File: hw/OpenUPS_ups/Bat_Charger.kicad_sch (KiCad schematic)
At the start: 23 parts, among them Q501 Q_PMOS_GDS, U501 MCP1415, U502 INA181A3, U503 MCP6001R, U504 MCP6001R

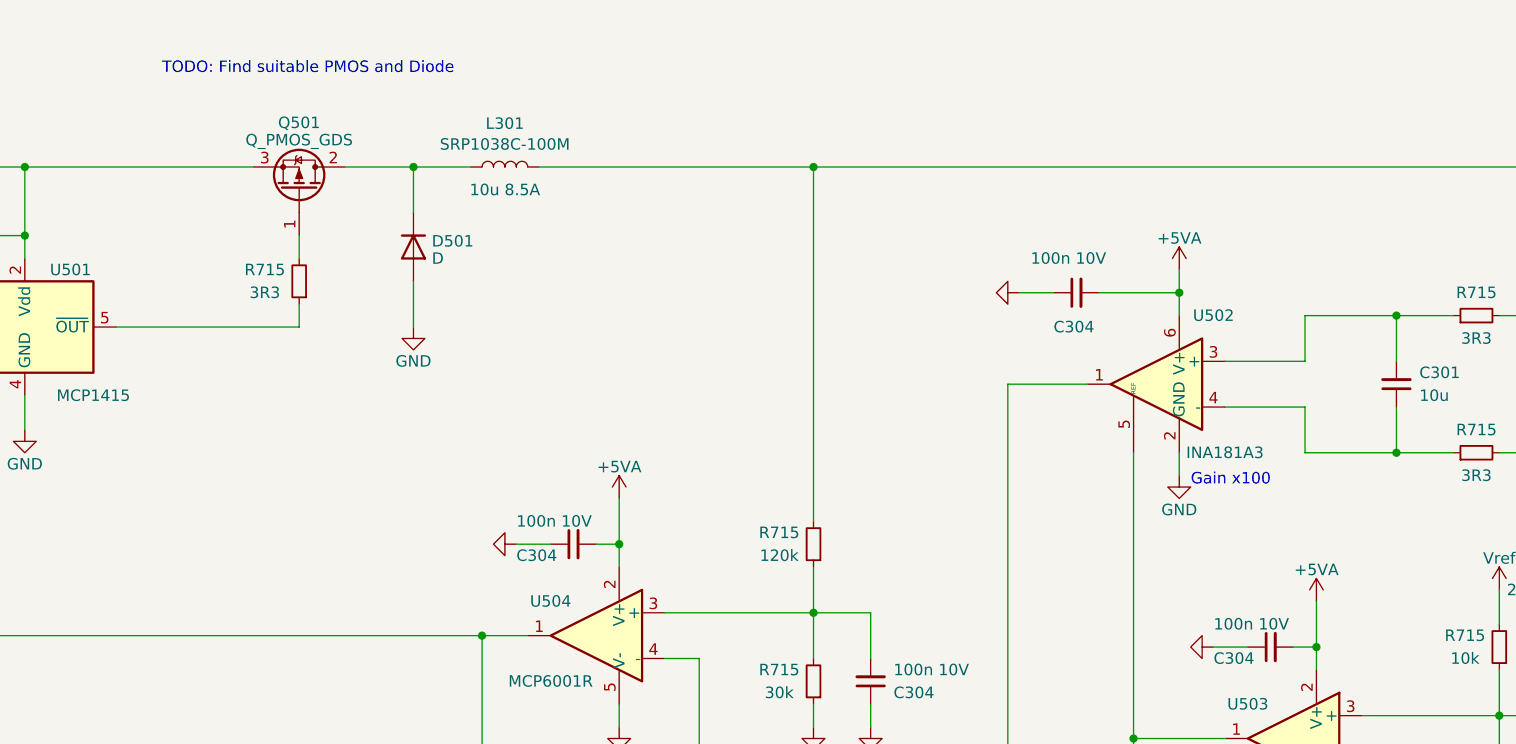
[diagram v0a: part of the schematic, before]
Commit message: Secondary blocks design
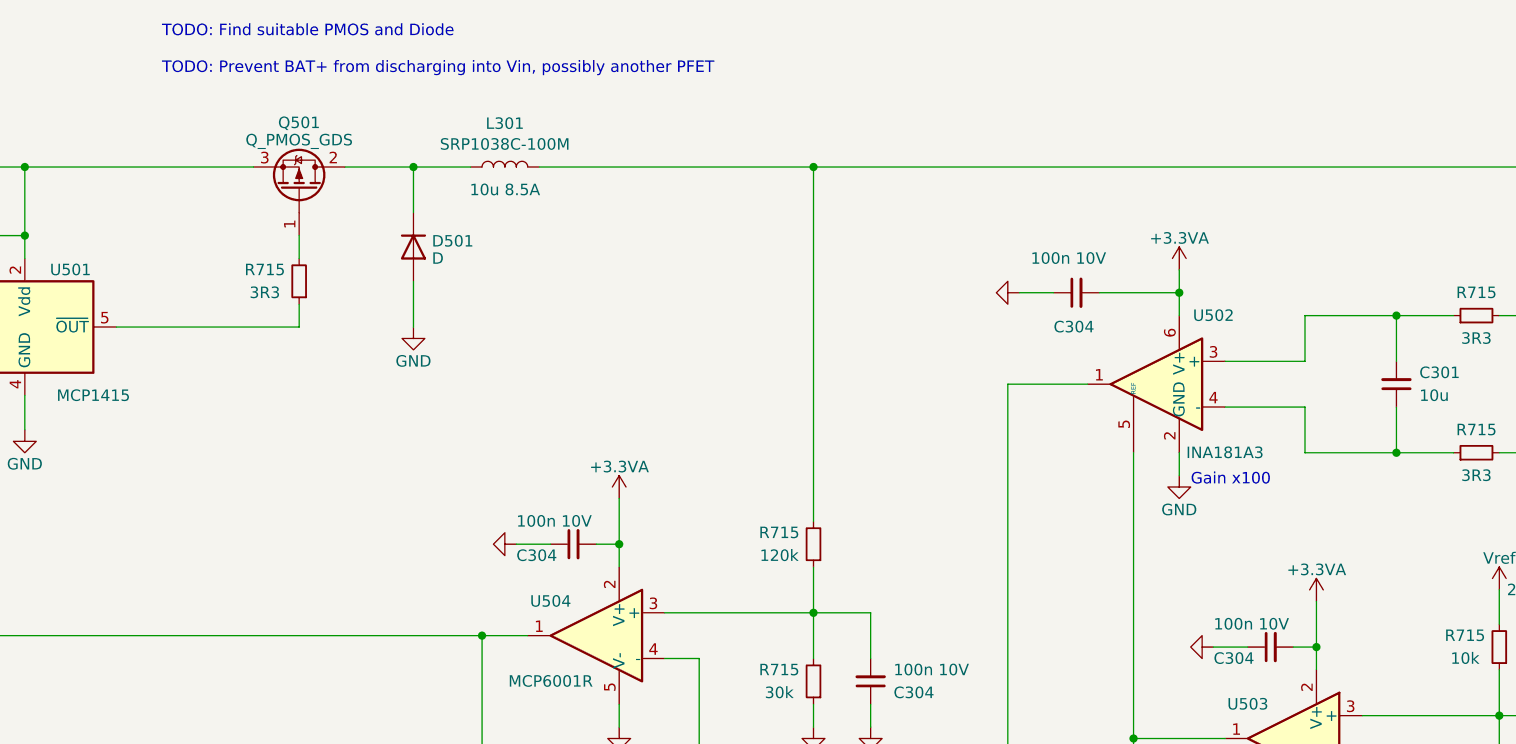
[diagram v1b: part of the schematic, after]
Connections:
- net +5VA renamed +3.3VA
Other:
- note added: "TODO: Find suitable PMOS and Diode TODO: Prevent BAT+ from discharging into Vin, possibly another PFET"
- note removed: "TODO: Find suitable PMOS and Diode"
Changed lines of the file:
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@@
     (effects (font (size 1.27 1.27)) (justify left bottom))
   )
-  (text "TODO: Find suitable PMOS and Diode" (at 95.25 62.23 0)
+  (text "TODO: Find suitable PMOS and Diode\n\nTODO: Prevent BAT+ from discharging into Vin, possibly another PFET"
+    (at 95.25 62.23 0)
     (effects (font (size 1.27 1.27)) (justify left bottom))
   )
@@
     )
   )
+  (symbol (lib_id "power:+3.3VA") (at 146.05 109.22 0) (unit 1)
+    (in_bom yes) (on_board yes) (dnp no) (fields_autoplaced)
+    (property "Reference" "#PWR0102" (at 146.05 113.03 0)
+      (effects (font (size 1.27 1.27)) hide)
+    )
+    (property "Value" "+3.3VA" (at 146.05 105.7181 0)
+      (effects (font (size 1.27 1.27)))
+    )
+    (property "Footprint" "" (at 146.05 109.22 0)
+      (effects (font (size 1.27 1.27)) hide)
+    )
+    (property "Datasheet" "" (at 146.05 109.22 0)
+      (effects (font (size 1.27 1.27)) hide)
+    )
+    (pin "1")
+    (instances
+      (project "OpenUPS_ups"
+        (path "/f77faec3-eac4-47f3-a2de-ec4a039f4502"
+          (reference "#PWR0102") (unit 1)
+        )
+        (path "/f77faec3-eac4-47f3-a2de-ec4a039f4502/0bd99307-a15c-41e8-997b-077d576f806c"
+          (reference "#PWR0431") (unit 1)
+        )
+      )
+    )
+  )
   (symbol (lib_id "power:GND") (at 190.5 86.36 270) (unit 1)
     (in_bom yes) (on_board yes) (dnp no)
@@
         (path "/f77faec3-eac4-47f3-a2de-ec4a039f4502/0bd99307-a15c-41e8-997b-077d576f806c"
           (reference "U504") (unit 1)
+        )
+      )
+    )
+  )
+  (symbol (lib_id "power:+3.3VA") (at 223.52 120.65 0) (unit 1)
+    (in_bom yes) (on_board yes) (dnp no) (fields_autoplaced)
+    (property "Reference" "#PWR0102" (at 223.52 124.46 0)
+      (effects (font (size 1.27 1.27)) hide)
+    )
+    (property "Value" "+3.3VA" (at 223.52 117.1481 0)
+      (effects (font (size 1.27 1.27)))
+    )
+    (property "Footprint" "" (at 223.52 120.65 0)
+      (effects (font (size 1.27 1.27)) hide)
+    )
+    (property "Datasheet" "" (at 223.52 120.65 0)
+      (effects (font (size 1.27 1.27)) hide)
+    )
+    (pin "1")
+    (instances
+      (project "OpenUPS_ups"
+        (path "/f77faec3-eac4-47f3-a2de-ec4a039f4502"
+          (reference "#PWR0102") (unit 1)
+        )
+        (path "/f77faec3-eac4-47f3-a2de-ec4a039f4502/0bd99307-a15c-41e8-997b-077d576f806c"
+          (reference "#PWR0433") (unit 1)
         )
       )
@@
     )
   )
+  (symbol (lib_id "power:+3.3VA") (at 208.28 83.82 0) (unit 1)
+    (in_bom yes) (on_board yes) (dnp no) (fields_autoplaced)
+    (property "Reference" "#PWR0102" (at 208.28 87.63 0)
+      (effects (font (size 1.27 1.27)) hide)
+    )
+    (property "Value" "+3.3VA" (at 208.28 80.3181 0)
+      (effects (font (size 1.27 1.27)))
+    )
+    (property "Footprint" "" (at 208.28 83.82 0)
+      (effects (font (size 1.27 1.27)) hide)
+    )
+    (property "Datasheet" "" (at 208.28 83.82 0)
+      (effects (font (size 1.27 1.27)) hide)
+    )
+    (pin "1")
+    (instances
+      (project "OpenUPS_ups"
+        (path "/f77faec3-eac4-47f3-a2de-ec4a039f4502"
+          (reference "#PWR0102") (unit 1)
+        )
+        (path "/f77faec3-eac4-47f3-a2de-ec4a039f4502/0bd99307-a15c-41e8-997b-077d576f806c"
+          (reference "#PWR0432") (unit 1)
+        )
+      )
+    )
+  )
   (symbol (lib_id "power:GND") (at 212.09 125.73 270) (unit 1)
     (in_bom yes) (on_board yes) (dnp no)
@@
         (path "/f77faec3-eac4-47f3-a2de-ec4a039f4502/0bd99307-a15c-41e8-997b-077d576f806c"
           (reference "#PWR0510") (unit 1)
-        )
-      )
-    )
-  )
-  (symbol (lib_id "power:+5VA") (at 146.05 109.22 0) (unit 1)
-    (in_bom yes) (on_board yes) (dnp no) (fields_autoplaced)
-    (property "Reference" "#PWR0516" (at 146.05 113.03 0)
-      (effects (font (size 1.27 1.27)) hide)
-    )
-    (property "Value" "+5VA" (at 146.05 105.7181 0)
-      (effects (font (size 1.27 1.27)))
-    )
-    (property "Footprint" "" (at 146.05 109.22 0)
-      (effects (font (size 1.27 1.27)) hide)
-    )
-    (property "Datasheet" "" (at 146.05 109.22 0)
-      (effects (font (size 1.27 1.27)) hide)
-    )
-    (pin "1")
-    (instances
-      (project "OpenUPS_ups"
-        (path "/f77faec3-eac4-47f3-a2de-ec4a039f4502/0bd99307-a15c-41e8-997b-077d576f806c"
-          (reference "#PWR0516") (unit 1)
         )
       )
@@
     )
   )
-  (symbol (lib_id "power:+5VA") (at 223.52 120.65 0) (unit 1)
-    (in_bom yes) (on_board yes) (dnp no) (fields_autoplaced)
-    (property "Reference" "#PWR0511" (at 223.52 124.46 0)
-      (effects (font (size 1.27 1.27)) hide)
-    )
-    (property "Value" "+5VA" (at 223.52 117.1481 0)
-      (effects (font (size 1.27 1.27)))
-    )
-    (property "Footprint" "" (at 223.52 120.65 0)
-      (effects (font (size 1.27 1.27)) hide)
-    )
-    (property "Datasheet" "" (at 223.52 120.65 0)
-      (effects (font (size 1.27 1.27)) hide)
-    )
-    (pin "1")
-    (instances
-      (project "OpenUPS_ups"
-        (path "/f77faec3-eac4-47f3-a2de-ec4a039f4502/0bd99307-a15c-41e8-997b-077d576f806c"
-          (reference "#PWR0511") (unit 1)
-        )
-      )
-    )
-  )
   (symbol (lib_id "Device:R_Small") (at 167.64 114.3 180) (unit 1)
     (in_bom yes) (on_board yes) (dnp no)
@@
         )
       )
-    )
-  )
-  (symbol (lib_id "power:+5VA") (at 208.28 83.82 0) (unit 1)
-    (in_bom yes) (on_board yes) (dnp no) (fields_autoplaced)
-    (property "Reference" "#PWR0512" (at 208.28 87.63 0)
-      (effects (font (size 1.27 1.27)) hide)
-    )
-    (property "Value" "+5VA" (at 208.28 80.3181 0)
-      (effects (font (size 1.27 1.27)))
-    )
-    (property "Footprint" "" (at 208.28 83.82 0)
-      (effects (font (size 1.27 1.27)) hide)
-    )
-    (property "Datasheet" "" (at 208.28 83.82 0)
-      (effects (font (size 1.27 1.27)) hide)
-    )
-    (pin "1")
-    (instances
-      (project "OpenUPS_ups"
-        (path "/f77faec3-eac4-47f3-a2de-ec4a039f4502/0bd99307-a15c-41e8-997b-077d576f806c"
-          (reference "#PWR0512") (unit 1)
-        )
-      )

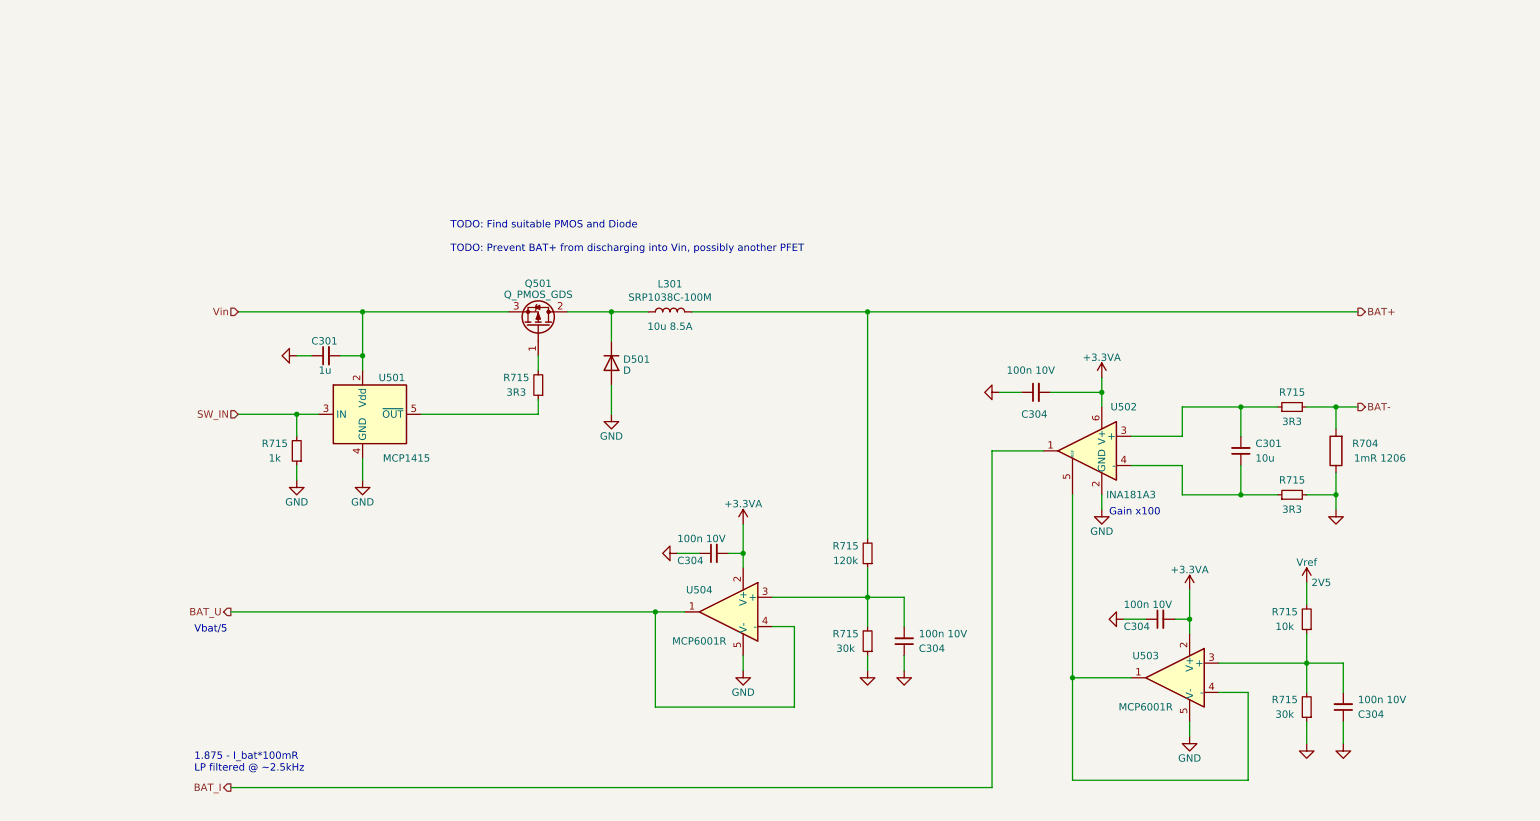
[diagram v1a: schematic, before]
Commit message: Upgraded battery charger with synchronous HB Driver
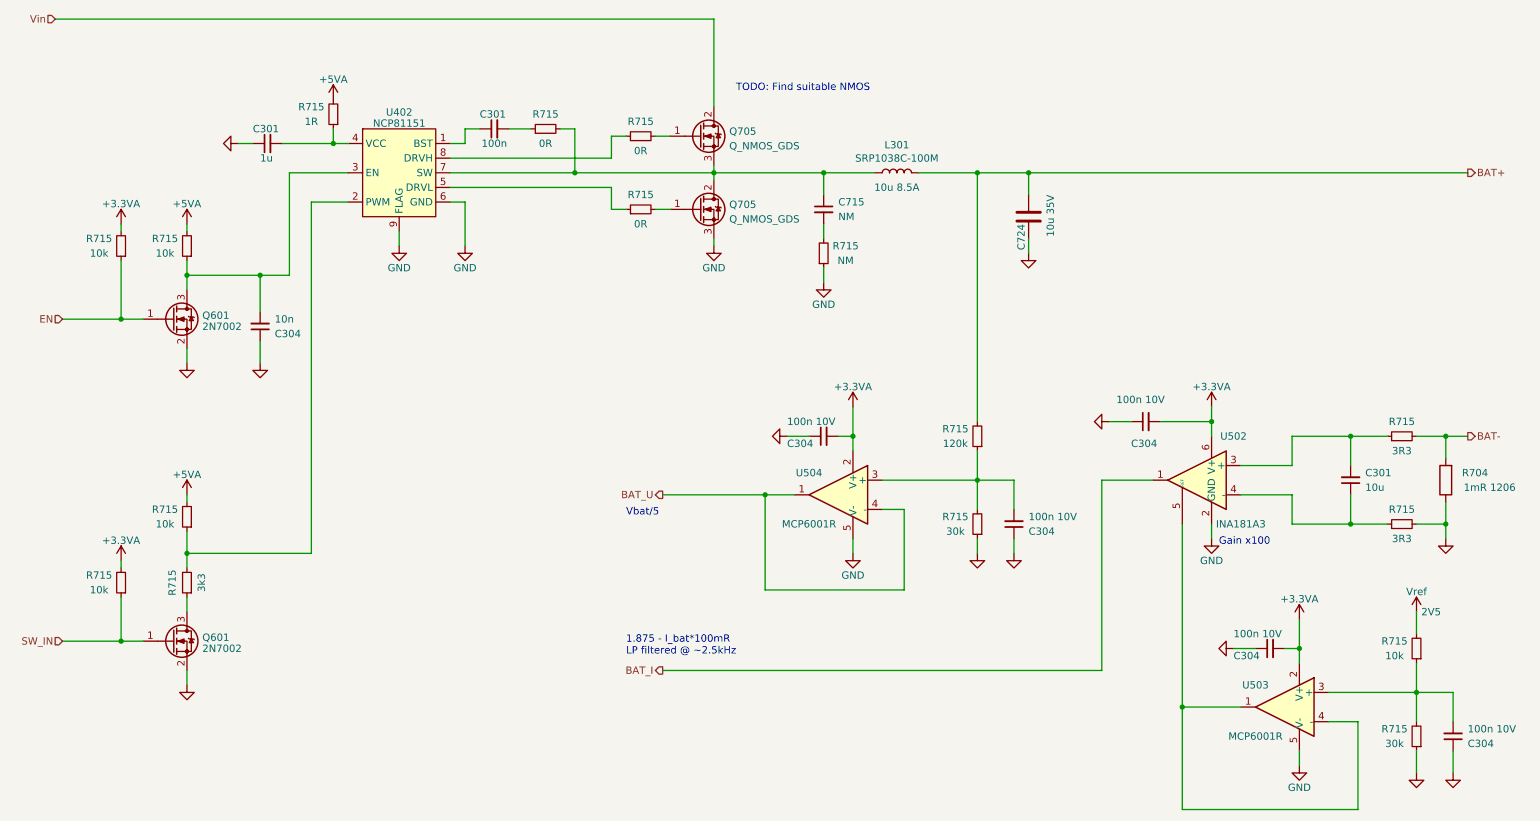
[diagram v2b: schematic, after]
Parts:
- removed D501: D, symbol Device:D
- removed Q501: Q_PMOS_GDS, symbol Device:Q_PMOS_GDS
- removed R715: 1k, Resistor_SMD:R_0603_1608Metric, symbol Device:R_Small
- removed R715: 3R3, Resistor_SMD:R_0603_1608Metric, symbol Device:R_Small
- removed U501: MCP1415, Package_TO_SOT_SMD:SOT-23-5, symbol Driver_FET:MCP1415
- added C301: 100n, Capacitor_SMD:C_0603_1608Metric, symbol Device:C_Small
- added C304: 10n, Capacitor_SMD:C_0603_1608Metric, symbol Device:C_Small
- added C715: NM, Capacitor_SMD:C_0603_1608Metric, symbol Device:C_Small
- added C724: 10u 35V, Capacitor_SMD:C_1206_3216Metric, symbol Device:C
- added Q601 (x2): 2N7002, Package_TO_SOT_SMD:SOT-23, symbol Transistor_FET:2N7002
- added Q705 (x2): Q_NMOS_GDS, Package_TO_SOT_SMD:TO-263-2, symbol Device:Q_NMOS_GDS
- added R715: NM, Resistor_SMD:R_0603_1608Metric, symbol Device:R_Small
- added R715 (x3): 0R, Resistor_SMD:R_0603_1608Metric, symbol Device:R_Small
- added R715: 1R, Resistor_SMD:R_0603_1608Metric, symbol Device:R_Small
- added R715 (x4): 10k, Resistor_SMD:R_0603_1608Metric, symbol Device:R_Small
- added R715: 3k3, Resistor_SMD:R_0603_1608Metric, symbol Device:R_Small
- added U402: NCP81151, Package_DFN_QFN:DFN-8-1EP_2x2mm_P0.5mm_EP0.9x1.3mm, symbol OpenUPS_ups:NCP81151
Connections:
- net +3.3VA: now also R715.2, R715.2
- net BAT+: now also C724.1
- net GND: now also C304.1, C724.2, Q601.2 (S), Q601.2 (S), Q705.3 (S), R715.1, U402.6 (GND), U402.9 (FLAG)
- net SW_IN: now also Q601.1 (G), R715.1
- net Vin: now also Q705.2 (D); no longer C301.2
- net at L301.1: now also C715.1, Q705.2 (D), Q705.3 (S), R715.2, U402.7 (SW)
- new net: C301.1, U402.1 (BST)
- new net: C301.2, R715.1
- new net: C304.2, Q601.3 (D), R715.1, U402.3 (EN)
- new net: C301.2, R715.1, U402.4 (VCC)
- new net: Q705.1 (G), R715.2 (x2)
- new net: C715.2, R715.2
- new net: R715.1, U402.5 (DRVL)
- new net: R715.1, U402.8 (DRVH)
- new net: R715.1, R715.2, U402.2 (PWM)
- new net: Q601.3 (D), R715.1
- new net +5VA: R715.2, R715.2, R715.2
- new net EN: Q601.1 (G), R715.1
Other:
- note added: "TODO: Find suitable NMOS"
- note removed: "TODO: Find suitable PMOS and Diode TODO: Prevent BAT+ from discharging into Vin, possibly another PFET"
- moved on the sheet: C301, C304, L301, R704, R715, U502, U503, U504
